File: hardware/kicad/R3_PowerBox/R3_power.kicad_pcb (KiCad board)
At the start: 4 copper layers, 160 x 80 mm, 202 parts, among them J1 SERVICE / BENCH INPUT 6-12V, J10 BATTERY / CHARGER TELEMETRY, J11 USER PANEL / PRIMARY ONLY, J12 PRIMARY B2B 2x8 / DNP, J13 ISOLATED B2B 2x5 / DNP, J2 DIGITAL POWER OUT, J3 ISOLATED POWER OUT, J4 CONTROL / SERVICE, J5 PRIMARY AUX DNP, J6 ISOLATED AUX DNP, J7 USB4105-GF-A, J8 2S BATTERY / KEYED / NTC_BMS=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, J9 NTC_CHG=103AT-2 / QUIET DGND 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, Q1 DMP3007LSS-13, Q2 CSD17577Q3AT 30V NMOS DSG, Q3 CSD17577Q3AT 30V NMOS CHG, Q4 DMP3007LSS-13 SYSTEM LOAD SWI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, SW1 C&K RS282G05A3 / POWER ON, SW2 QON SERVICE / TL3305AF160QG, U1 TPS62132RGTR, U10 STUSB4500QTR, U11 BQ294502 SPACE ONLY / NC / DNP, U2 TPS54302DDCR, U3 RS3E-0505S/H3, U4 ADM7150ACPZ-3.3-R7, U5 TPS7A2033PDBVR, U6 RS3-0505D/H3, U7 TPS2121RUXR, U8 BQ25798RQM, U9 BQ28Z610DRZR

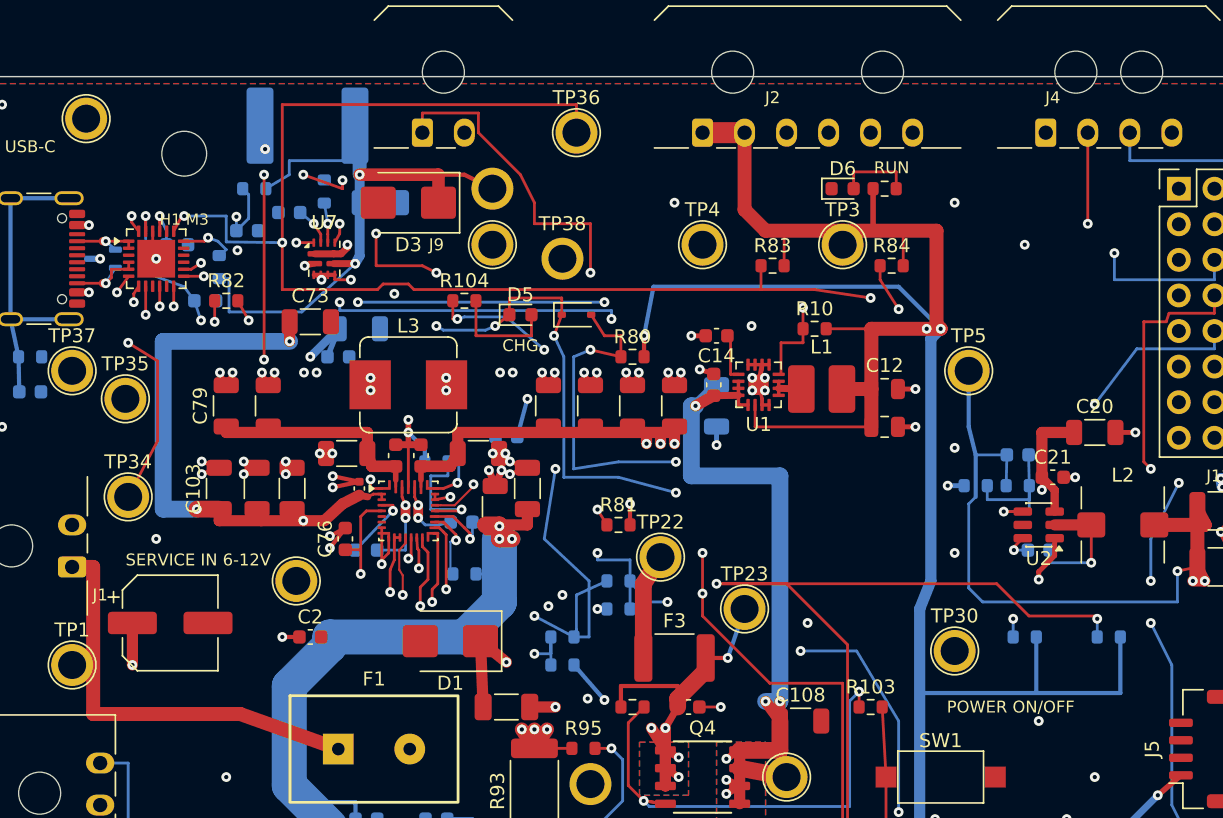
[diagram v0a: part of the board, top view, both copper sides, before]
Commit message: Rev.A review fixes: final CAD verification and documented hardware gates
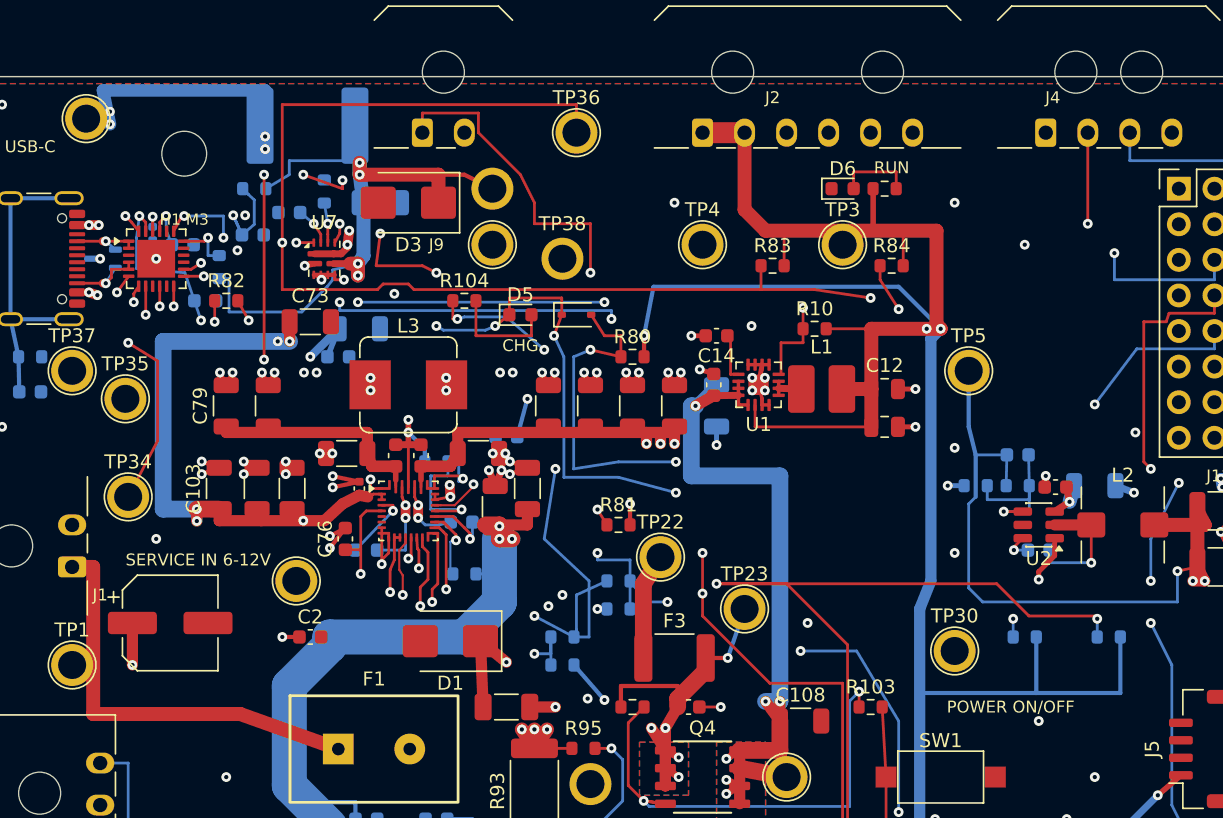
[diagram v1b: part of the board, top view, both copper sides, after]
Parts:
- added C109: 1uF/10V PD VSYS, Capacitor_SMD:C_0402_1005Metric, B.Cu at (32.8, 31.2)
- C20: moved to B.Cu
- R76: value 243k ILIM TOP / DEFAULT 0.50A -> 28.7k 0.1% ILIM TOP / SAFE START
- R77: value 100k ILIM BOT -> 10k 0.1% ILIM BOT
- moved C20 3.80 mm to (100.0, 49.2)
- moved C21 0.73 mm to (97.2, 49.3), turned to 180 degrees
- moved C106 0.50 mm to (39.9, 31.3)
- moved C104 0.40 mm to (34.9, 32.0)
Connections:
- U10 pad 22: DGND -> +3V3_D
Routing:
- net USB_VBUS_RAW: track 44.2 -> 58.8 mm, vias 3 -> 8
- net +3V3_D: track 349.5 -> 360.2 mm, vias 6 -> 8
- net VSYS_MAIN: track 101.6 -> 94.2 mm
- net CHARGER_IN: track 80.1 -> 85.5 mm, vias 5 -> 8
- net USB_VBUS_PROT: track 45.6 -> 49.8 mm, vias 2 -> 4
- net PD_ALERT_N: track 213.2 -> 215.7 mm, vias 4 -> 5
- net PD_VDD: track 36.8 -> 39.3 mm
- net PACK_POS: track 114.5 -> 116.2 mm, vias 9 -> 10
- net N$9: track 7.68 -> 9.32 mm
- net PD_VREG_2V7: track 19.8 -> 21.1 mm
- net DGND: track 100.4 -> 99.9 mm, vias 89 -> 90

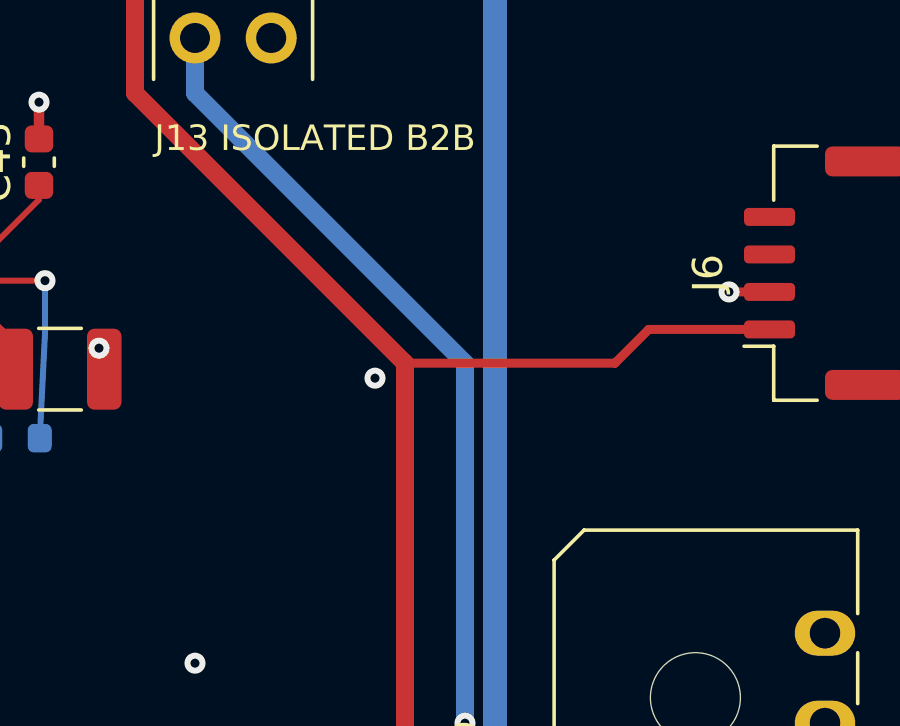
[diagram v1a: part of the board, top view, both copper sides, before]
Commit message: Add Garage Logic Lab silk and prototype fabrication export
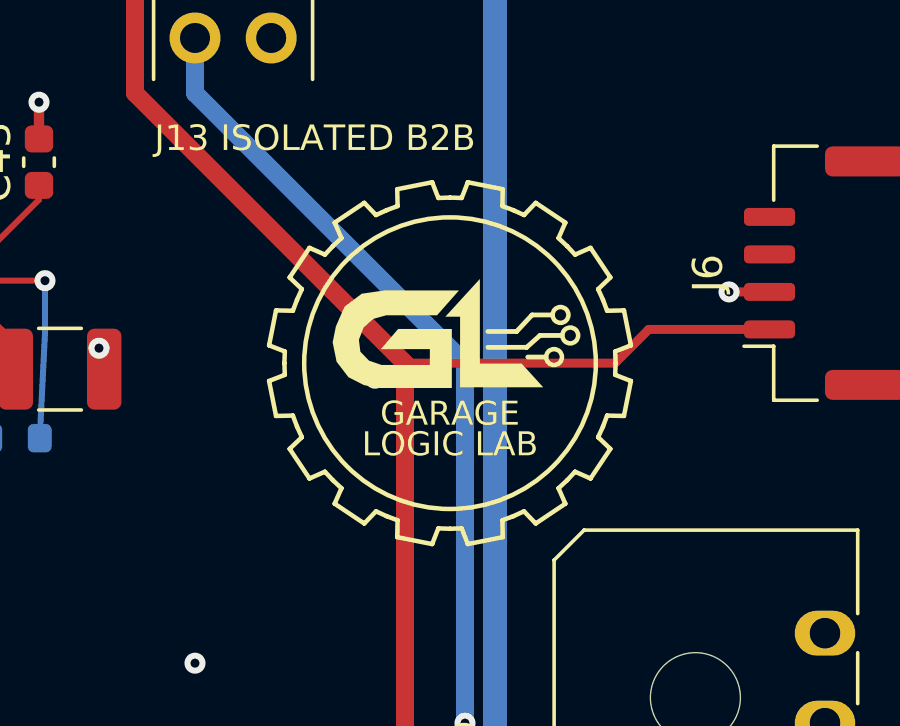
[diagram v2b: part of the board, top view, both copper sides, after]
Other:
- board text added: "GARAGE"
- board text added: "LOGIC LAB"

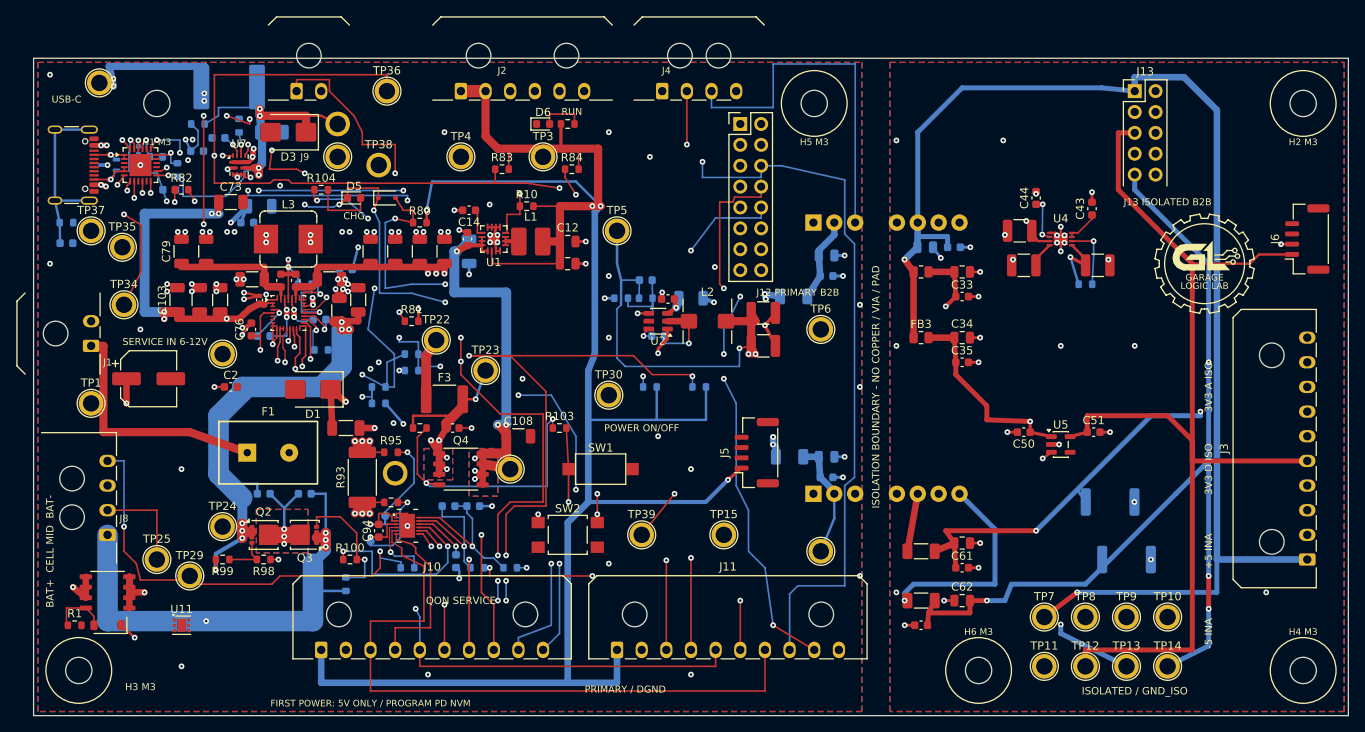
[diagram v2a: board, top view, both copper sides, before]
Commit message: Fix U4 physical pin numbering and checkpoint local orientation repair
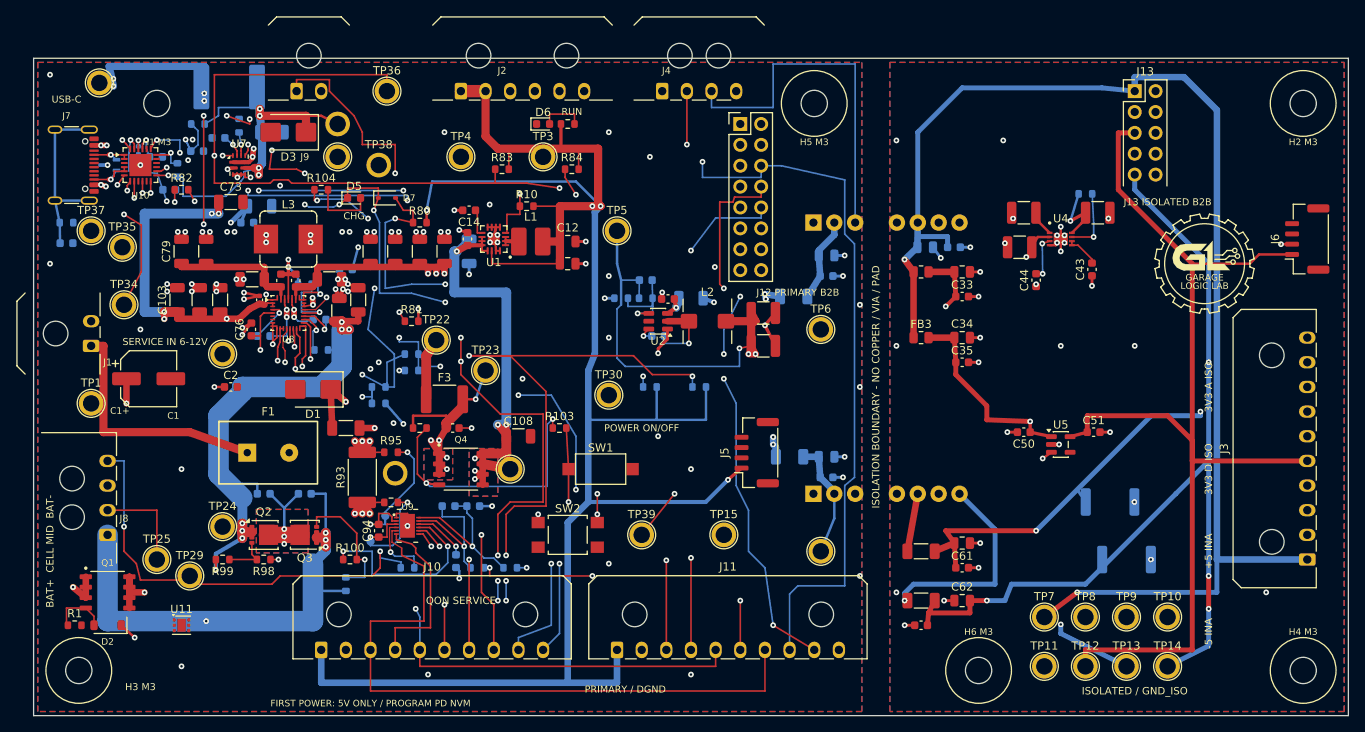
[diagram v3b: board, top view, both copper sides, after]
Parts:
- moved R40 11.0 mm to (148.0, 36.5)
- moved C44 10.0 mm to (142.0, 47.0), turned to -90 degrees
- moved C43 7.40 mm to (148.8, 45.7), turned to -90 degrees
- moved C40 6.40 mm to (149.5, 38.8)
- moved C41 6.40 mm to (140.5, 38.8)
- moved C42 2.00 mm to (140.0, 43.0)
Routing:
- net +5V_ISO_A: track 83.9 -> 93.0 mm
- net +3V3_A_ISO: track 149.4 -> 153.8 mm
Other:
- board text added: "C1+"
